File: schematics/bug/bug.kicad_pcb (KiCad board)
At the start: 2 copper layers, 15 parts, among them P1 CONN_01X09, P2 CONN_01X04, P3 CONN_01X06, P4 CONN_01X02, U1 uln2803A, U2 Arduino_Mini, U3 SPX2920U-3.3, U4 ESP8266

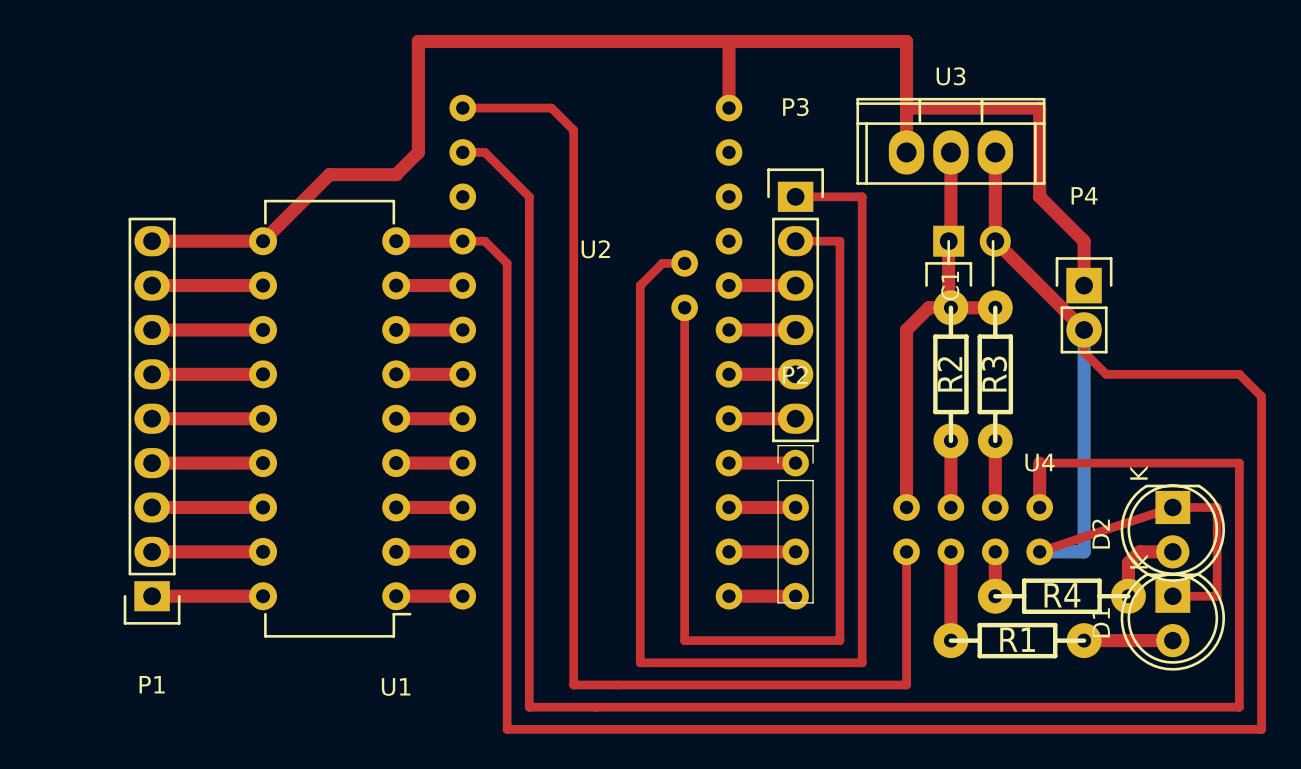
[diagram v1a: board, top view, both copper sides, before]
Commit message: Update bug schematic
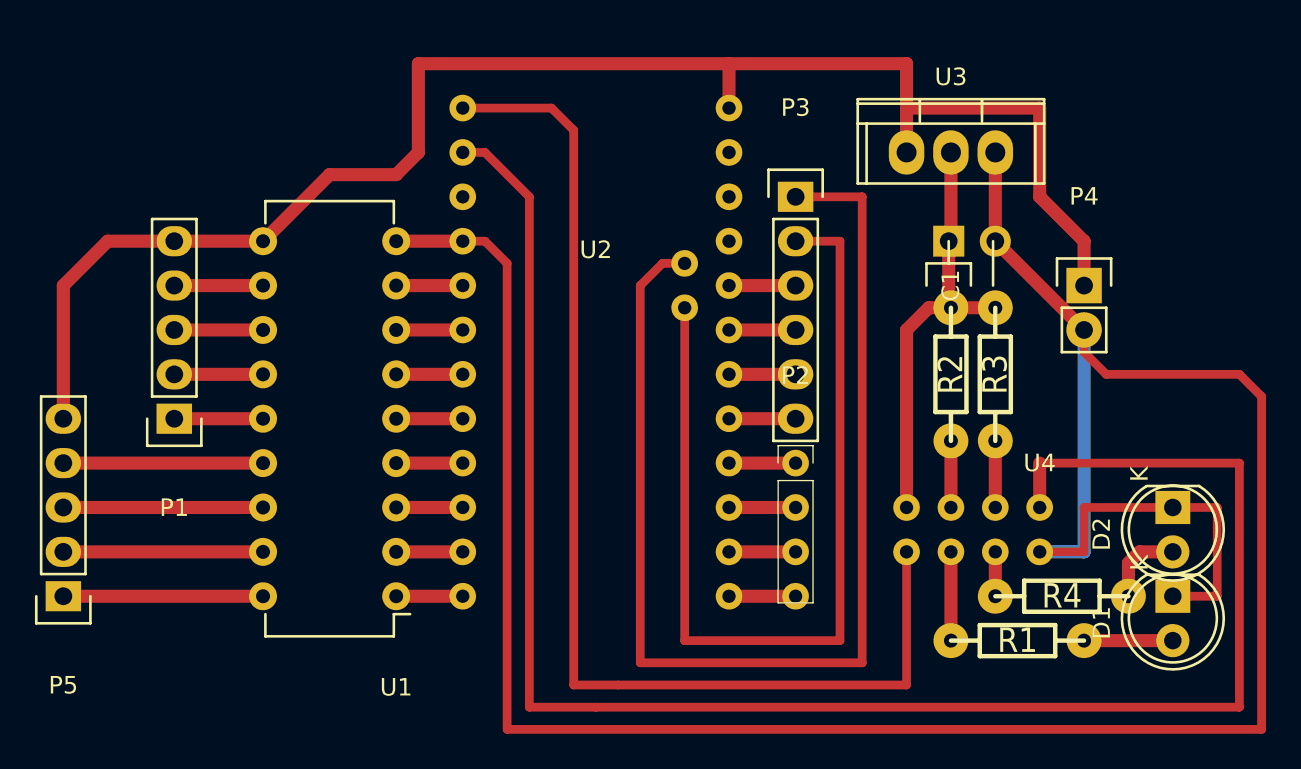
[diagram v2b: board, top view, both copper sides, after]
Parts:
- added P5: CONN_01X05, Pin_Headers:Pin_Header_Straight_1x05, F.Cu at (109.2, 124.5)
- P1: value CONN_01X09 -> CONN_01X05; footprint Pin_Headers:Pin_Header_Straight_1x09 -> Pin_Headers:Pin_Header_Straight_1x05
- moved P1 10.2 mm to (115.6, 114.3)
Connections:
- P4 pad 1: Net-(P1-Pad9) -> Net-(P1-Pad5)
- U1 pad 10: Net-(P1-Pad9) -> Net-(P1-Pad5)
- U1 pad 11: Net-(P1-Pad8) -> Net-(P1-Pad4)
- U1 pad 12: Net-(P1-Pad7) -> Net-(P1-Pad3)
- U1 pad 13: Net-(P1-Pad6) -> Net-(P1-Pad2)
- U1 pad 14: Net-(P1-Pad5) -> Net-(P1-Pad1)
- U1 pad 15: Net-(P1-Pad4) -> Net-(P5-Pad4)
- U1 pad 16: Net-(P1-Pad3) -> Net-(P5-Pad3)
- U1 pad 17: Net-(P1-Pad2) -> Net-(P5-Pad2)
- U1 pad 18: Net-(P1-Pad1) -> Net-(P5-Pad1)
- U2 pad 7: Net-(P1-Pad9) -> Net-(P1-Pad5)
- U3 pad 1: Net-(P1-Pad9) -> Net-(P1-Pad5)
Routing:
- net Net-(P1-Pad5): track 6.35 -> 90.6 mm
- net Net-(P1-Pad9): track 80.6 -> 0.00 mm
- net Net-(P5-Pad4): track 0.00 -> 11.4 mm
- net Net-(P5-Pad3): track 0.00 -> 11.4 mm
- net Net-(P5-Pad2): track 0.00 -> 11.4 mm
- net Net-(P5-Pad1): track 0.00 -> 11.4 mm
- net Net-(P1-Pad8): track 6.35 -> 0.00 mm
- net Net-(P1-Pad7): track 6.35 -> 0.00 mm
- net Net-(P1-Pad6): track 6.35 -> 0.00 mm
- net Net-(C1-Pad2): track 154.5 -> 156.6 mm
- net Net-(P1-Pad4): track 6.35 -> 5.08 mm
- net Net-(P1-Pad3): track 6.35 -> 5.08 mm
- net Net-(P1-Pad2): track 6.35 -> 5.08 mm
- net Net-(P1-Pad1): track 6.35 -> 5.08 mm
